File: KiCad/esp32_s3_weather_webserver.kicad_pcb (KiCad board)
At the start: 4 copper layers, 85 x 75 mm, 128 parts, among them IC301 CP2102N-A02-GQFN28R, IC401 ESP32-S3-WROOM-1-N16R8, IC501 VEML7700-TT, IC502 DS3231MZ+TRL, J201 Barrel_Jack_Switch_Pin3Ring, J301 USB_C_Receptacle_USB2.0, J302 USB_C_Receptacle_USB2.0, J401 Conn_01x04_Pin, J402 Conn_01x04_Pin, J403 Conn_01x04_Pin, J404 TF-01A, J405 Conn_01x08_Pin, Q401 SS8050, Q402 SS8050, U201 AMS1117-3.3, U202 TLV62569DBV, U301 USBLC6-2SC6, U302 USBLC6-2SC6, U502 DS18B20, U503 LM35-LP, U504 DHT11

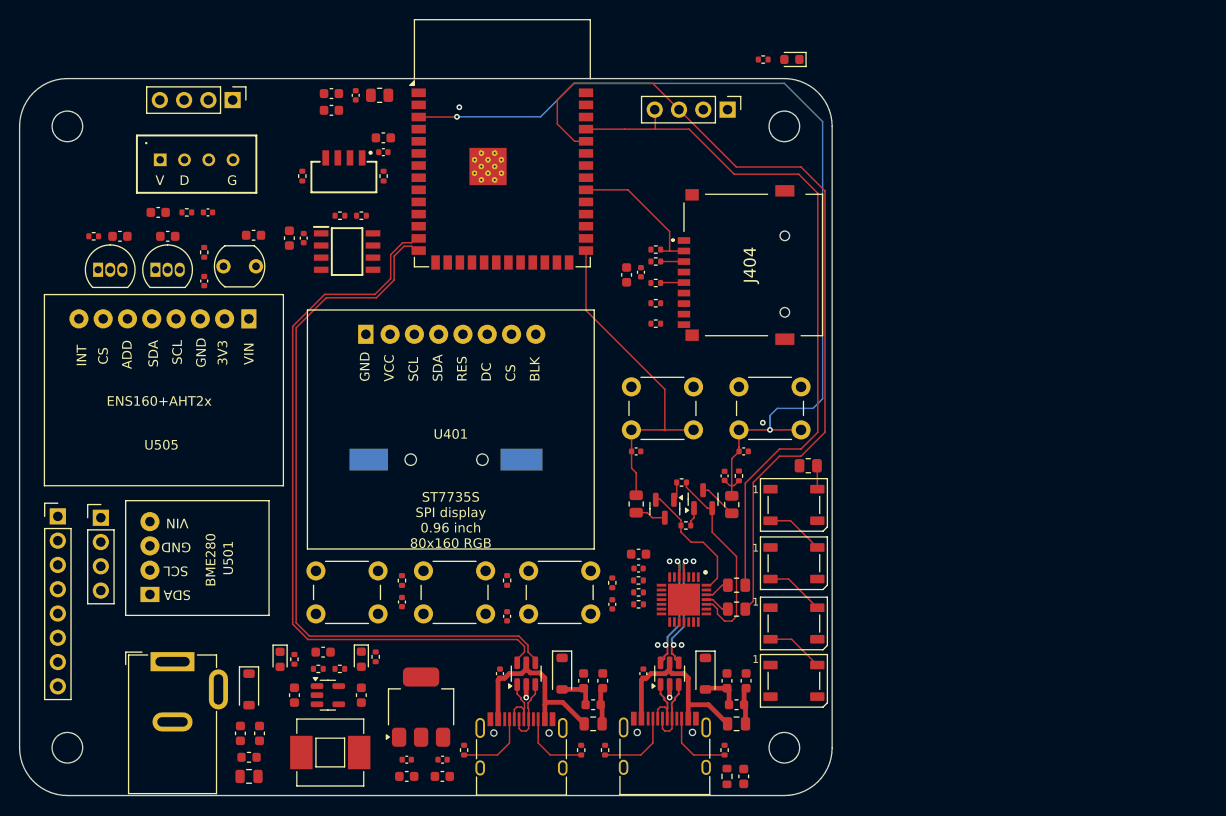
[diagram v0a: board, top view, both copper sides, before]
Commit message: SPI signals routing
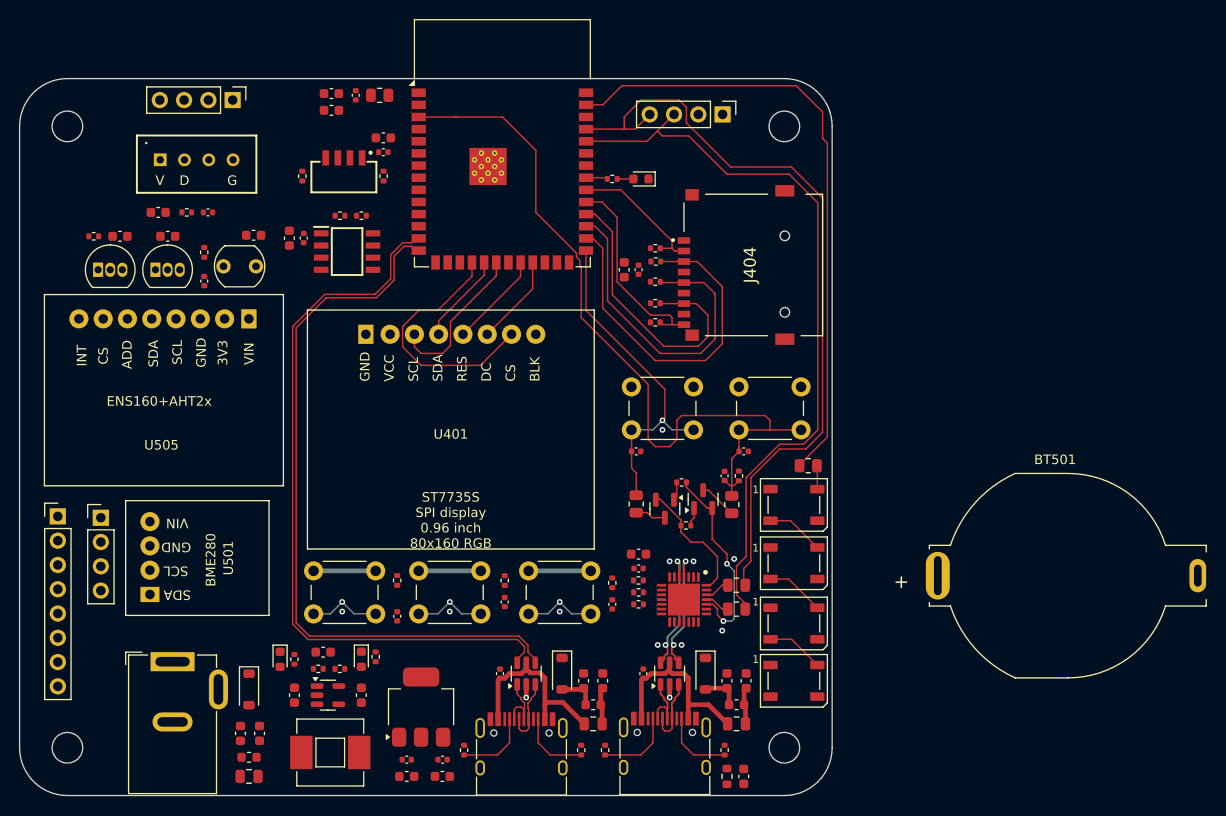
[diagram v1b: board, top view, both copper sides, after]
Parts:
- BT501: footprint esp32_s3_weather_webserver:CR12202 -> esp32_s3_weather_webserver:MPD_BC2032-E2; moved to F.Cu
- moved BT501 66.3 mm to (134.7, 77.0)
- moved D210 20.1 mm to (90.0, 35.5)
- moved R206 20.1 mm to (87.0, 35.5)
- moved C512 11.5 mm to (64.5, 81.2)
- moved R509 11.5 mm to (64.5, 77.5)
- moved SW502 11.5 mm to (55.8, 76.5)
- moved C511 10.8 mm to (75.8, 79.8)
- moved R508 10.8 mm to (75.8, 77.5)
- moved SW501 10.8 mm to (66.8, 76.5)
- moved J402 0.72 mm to (98.5, 28.8)
- moved C407 0.59 mm to (88.2, 45.0), turned to -90 degrees
- moved C408 0.36 mm to (89.8, 45.0), turned to -90 degrees
- moved R411 0.14 mm to (91.5, 46.2)
- moved R412 0.14 mm to (91.5, 42.8)
- moved R413 0.14 mm to (91.5, 50.5)
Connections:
- IC401 pad 10: USR_BTN_LEFT -> ENS160_INT
- IC401 pad 11: USR_BTN_RIGHT -> DS3231_INT
- IC401 pad 22: ENS160_INT -> TFT_RES
- IC401 pad 23: SD_CD -> TFT_DC
- IC401 pad 25: WS2812_RGB_STRIP -> USR_BTN
- IC401 pad 31: ONBOARD_LED -> SD_CD
- IC401 pad 33: TFT_RES -> ONBOARD_LED
- IC401 pad 34: TFT_DC -> USR_BTN_RIGHT
- IC401 pad 35: DS3231_INT -> USR_BTN_LEFT
- IC401 pad 39: USR_BTN -> WS2812_RGB_STRIP
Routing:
- net WS2812_RGB_STRIP: track 0.00 -> 65.1 mm
- net FSPI_MOSI: track 2.44 -> 37.5 mm
- net FSPI_SCK: track 2.46 -> 34.5 mm
- net FSPI_MISO: track 0.00 -> 30.5 mm
- net HSPI_SS: track 0.00 -> 26.5 mm
- net SD_CD: track 0.00 -> 21.3 mm
- net +3V3_PER: track 0.00 -> 19.5 mm
- net HSPI_SCK: track 0.00 -> 16.4 mm
- net /[4] ESP32 S3/CHIP_PU: track 97.7 -> 81.5 mm, vias 2 -> 0
- net /[4] ESP32 S3/RXD0: track 88.2 -> 78.1 mm
- net TFT_RES: track 0.00 -> 10.0 mm
- net TFT_DC: track 0.00 -> 9.48 mm
- net HSPI_MOSI: track 0.00 -> 9.48 mm
- net USR_BTN_RIGHT: track 0.00 -> 7.54 mm, vias 0 -> 1
- net USR_BTN_LEFT: track 0.00 -> 7.54 mm, vias 0 -> 1
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
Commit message: Simple signal routing
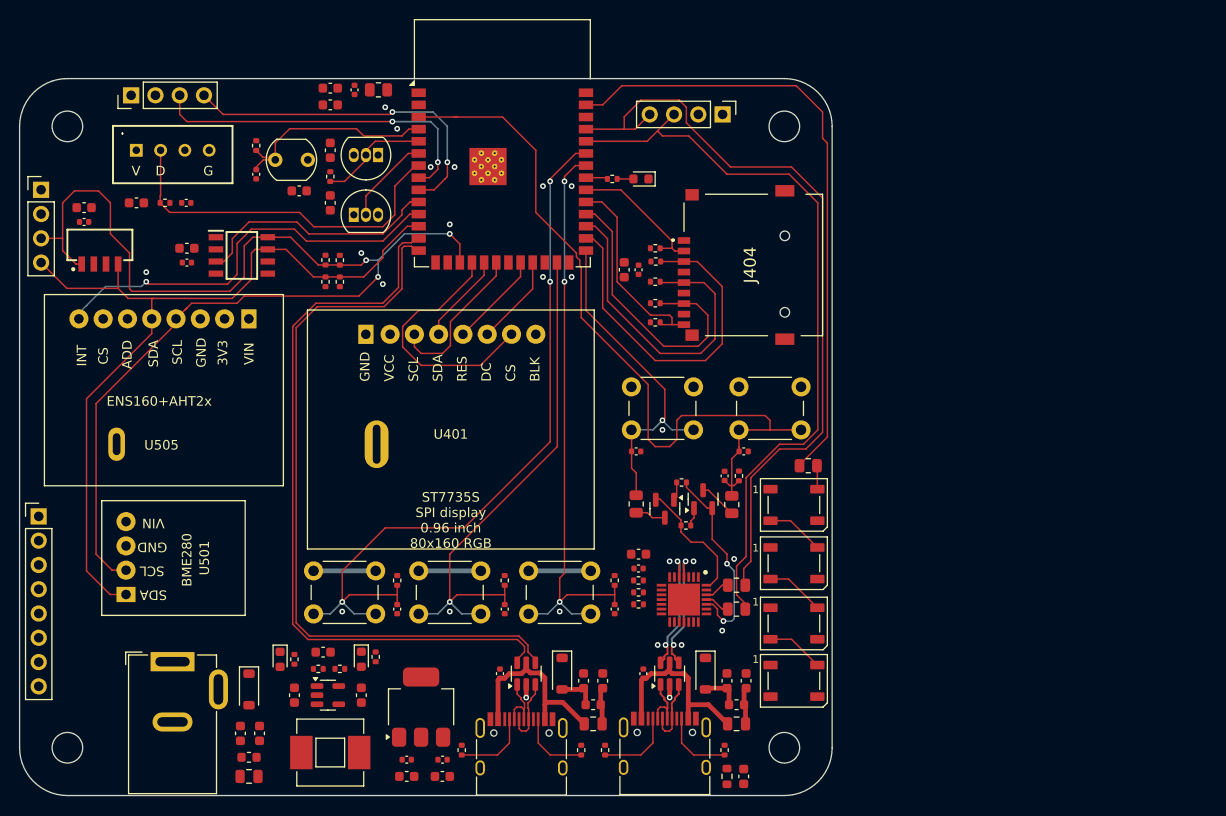
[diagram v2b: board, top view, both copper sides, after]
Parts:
- BT501: moved to B.Cu
- moved BT501 87.0 mm to (48.8, 63.2), turned to 180 degrees
- moved J403 34.9 mm to (27.2, 36.6)
- moved IC501 33.9 mm to (30.0, 44.0), turned to 0 degrees
- moved C503 32.1 mm to (31.8, 38.5)
- moved C504 32.1 mm to (31.8, 40.0)
- moved U502 31.7 mm to (62.5, 33.0), turned to 180 degrees
- moved R504 25.5 mm to (57.5, 35.2), turned to -90 degrees
- moved C505 23.8 mm to (57.5, 32.5), turned to 90 degrees
- moved U503 21.5 mm to (60.0, 39.2)
- moved C506 17.4 mm to (57.5, 38.0), turned to 90 degrees
- moved C508 12.5 mm to (42.5, 44.2), turned to 0 degrees
- moved C502 12.4 mm to (49.8, 35.0)
- moved R501 12.4 mm to (49.8, 32.0)
- moved RLO501 12.4 mm to (51.8, 33.5)
- moved R503 11.3 mm to (57.0, 46.3)
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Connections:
- IC401 pad 10: ENS160_INT -> DS3231_INT
- IC401 pad 11: DS3231_INT -> ENS160_INT
- J403 pad 3: I2C_SDA -> I2C_SCL
- J403 pad 4: I2C_SCL -> I2C_SDA
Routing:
- net I2C_SCL: track 0.00 -> 126.7 mm, vias 0 -> 3
- net I2C_SDA: track 0.00 -> 87.8 mm
- net USR_BTN_LEFT: track 7.54 -> 78.7 mm, vias 1 -> 3
- net USR_BTN_RIGHT: track 7.54 -> 63.0 mm, vias 1 -> 3
- net USR_BTN: track 7.54 -> 55.8 mm
- net ENS160_INT: track 0.00 -> 43.6 mm, vias 0 -> 1
- net DHT11: track 0.00 -> 38.0 mm
- net RXD1: track 0.00 -> 36.2 mm, vias 0 -> 2
- net TXD1: track 0.00 -> 35.8 mm, vias 0 -> 2
- net DS3231_INT: track 0.00 -> 26.0 mm
- net LDR: track 0.00 -> 23.0 mm
- net DS18B20: track 0.00 -> 11.6 mm
- net LM35: track 0.00 -> 9.34 mm
- net USB_D+: track 76.2 -> 77.3 mm
- net USB_D-: track 76.8 -> 77.9 mm
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
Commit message: Signals routing
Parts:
- moved D209 19.0 mm to (33.2, 84.5)
- moved R205 19.0 mm to (34.8, 84.5)
- moved D201 18.8 mm to (67.8, 89.2)
- moved F201 18.8 mm to (67.8, 98.2)
- moved FB201 18.8 mm to (67.8, 96.2)
- moved J201 18.8 mm to (59.8, 86.2)
- moved C205 18.7 mm to (68.8, 93.8)
- moved C206 18.7 mm to (66.8, 93.8)
- moved C202 18.0 mm to (51.2, 96.5), turned to 180 degrees
- moved C203 18.0 mm to (47.5, 96.5), turned to 0 degrees
- moved C204 18.0 mm to (47.5, 98.2), turned to 0 degrees
- moved C207 18.0 mm to (42.8, 89.8)
- moved C208 18.0 mm to (35.8, 89.8)
- moved C209 18.0 mm to (38.8, 85.2)
- moved L201 18.0 mm to (39.5, 95.8)
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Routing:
- net +5V: track 0.00 -> 250.2 mm, vias 0 -> 10
- net +3V3: track 0.00 -> 55.9 mm
- net GNDPWR: track 0.00 -> 44.4 mm
- net GND: track 2.72 -> 46.1 mm, vias 24 -> 80
- net +3V3_PER: track 19.5 -> 60.7 mm
- net /[5] Peripherals/VBAT: track 0.00 -> 32.2 mm, vias 0 -> 1
- net +VCC_USB2UART_FILT: track 4.11 -> 21.8 mm
- net +5V_IN: track 0.00 -> 16.0 mm
- net I2C_SCL: track 126.7 -> 113.2 mm, vias 3 -> 4
- net +5V_IN_FILT: track 0.00 -> 9.65 mm
- net /[2] Power/BUCK_FB: track 0.00 -> 5.45 mm
- net I2C_SDA: track 87.8 -> 92.2 mm
- net +5V_IN_FUSE: track 0.00 -> 3.88 mm
- net /[3] USB/VBUS: track 0.00 -> 3.14 mm
- net /[3] USB/RSTB: track 0.00 -> 2.95 mm
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- added copper zone on F.Cu, net +3V3_PER
- added copper zone on F.Cu, net /[2] Power/BUCK_SW

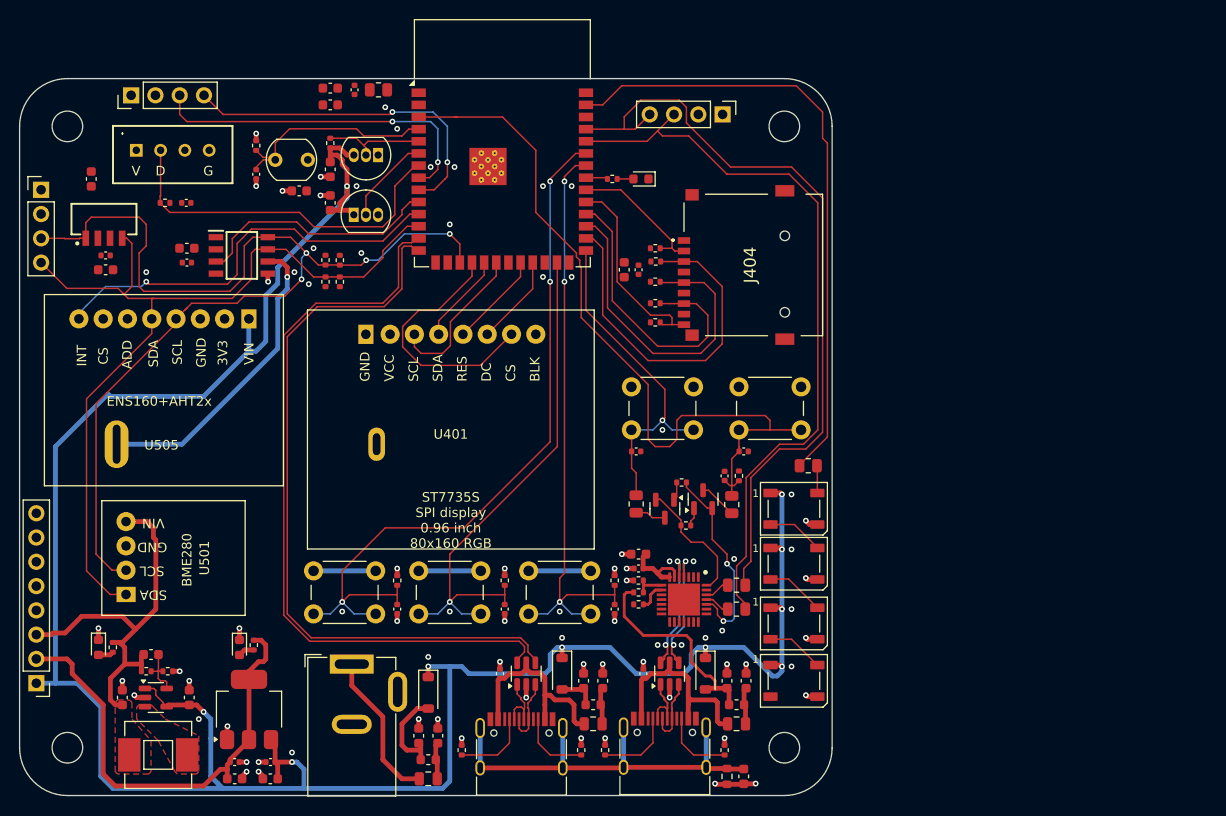
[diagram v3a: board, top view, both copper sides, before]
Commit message: Signal routing
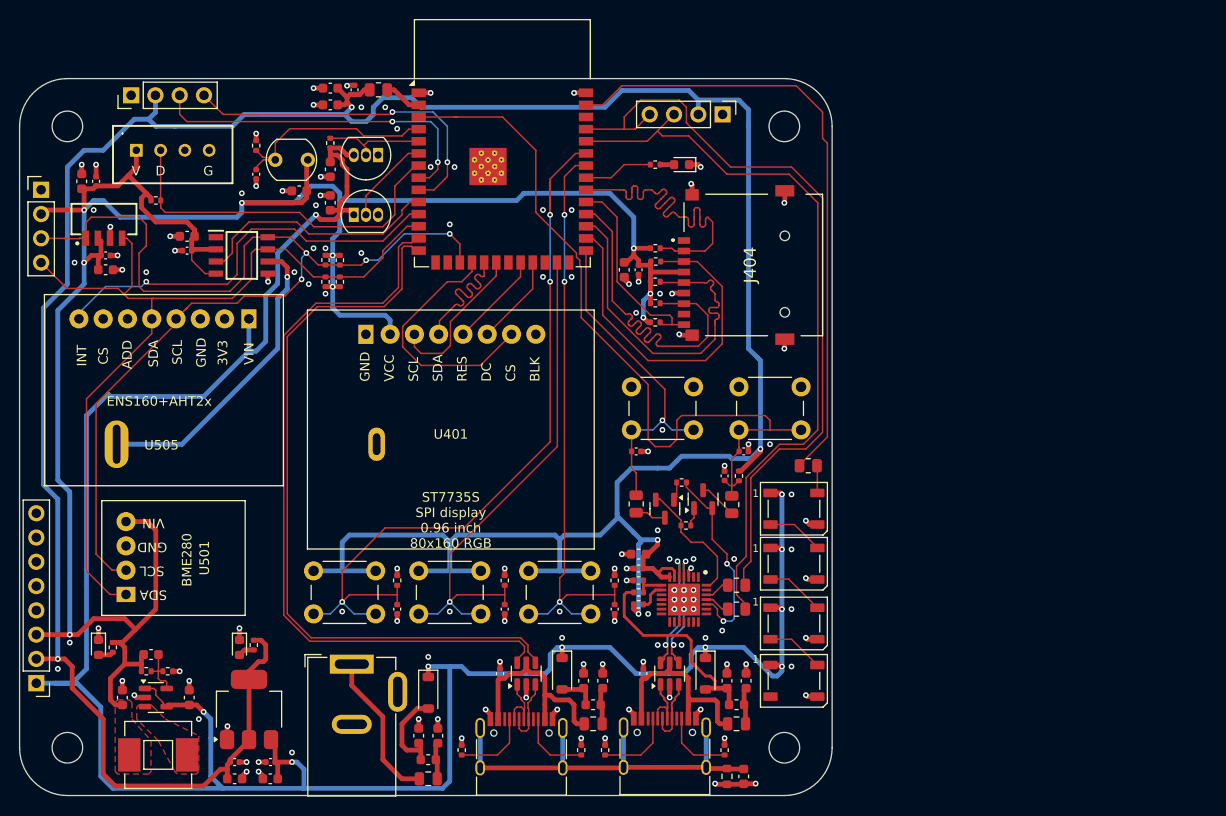
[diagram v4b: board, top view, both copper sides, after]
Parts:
- moved C510 9.70 mm to (33.0, 35.8), turned to 90 degrees
- moved R206 4.73 mm to (91.5, 34.0)
- moved D210 4.51 mm to (94.2, 34.0)
- moved C507 1.25 mm to (42.5, 41.5), turned to 180 degrees
- moved C508 1.25 mm to (42.5, 43.0), turned to 180 degrees
- moved C509 1.03 mm to (31.5, 35.8)
- moved R505 1.00 mm to (39.2, 37.8), turned to 0 degrees
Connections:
- SW501 pad 1: +3V3_PER -> +3V3
- SW501 pad 4: +3V3_PER -> +3V3
- SW502 pad 1: +3V3_PER -> +3V3
- SW502 pad 4: +3V3_PER -> +3V3
- SW503 pad 1: +3V3_PER -> +3V3
- SW503 pad 4: +3V3_PER -> +3V3
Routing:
- net +3V3: track 55.9 -> 334.3 mm, vias 0 -> 5
- net +3V3_PER: track 60.7 -> 246.9 mm, vias 0 -> 9
- net GND: track 46.1 -> 75.5 mm, vias 80 -> 130
- net FSPI_SS: track 14.6 -> 38.7 mm
- net FSPI_MISO: track 30.9 -> 37.6 mm
- net HSPI_MOSI: track 9.48 -> 15.5 mm
- net ONBOARD_LED: track 2.29 -> 7.30 mm
- net +3V3_ESP32: track 0.00 -> 3.95 mm
- net USR_BTN_LEFT: track 78.7 -> 82.1 mm
- net FSPI_SCK: track 35.0 -> 38.1 mm

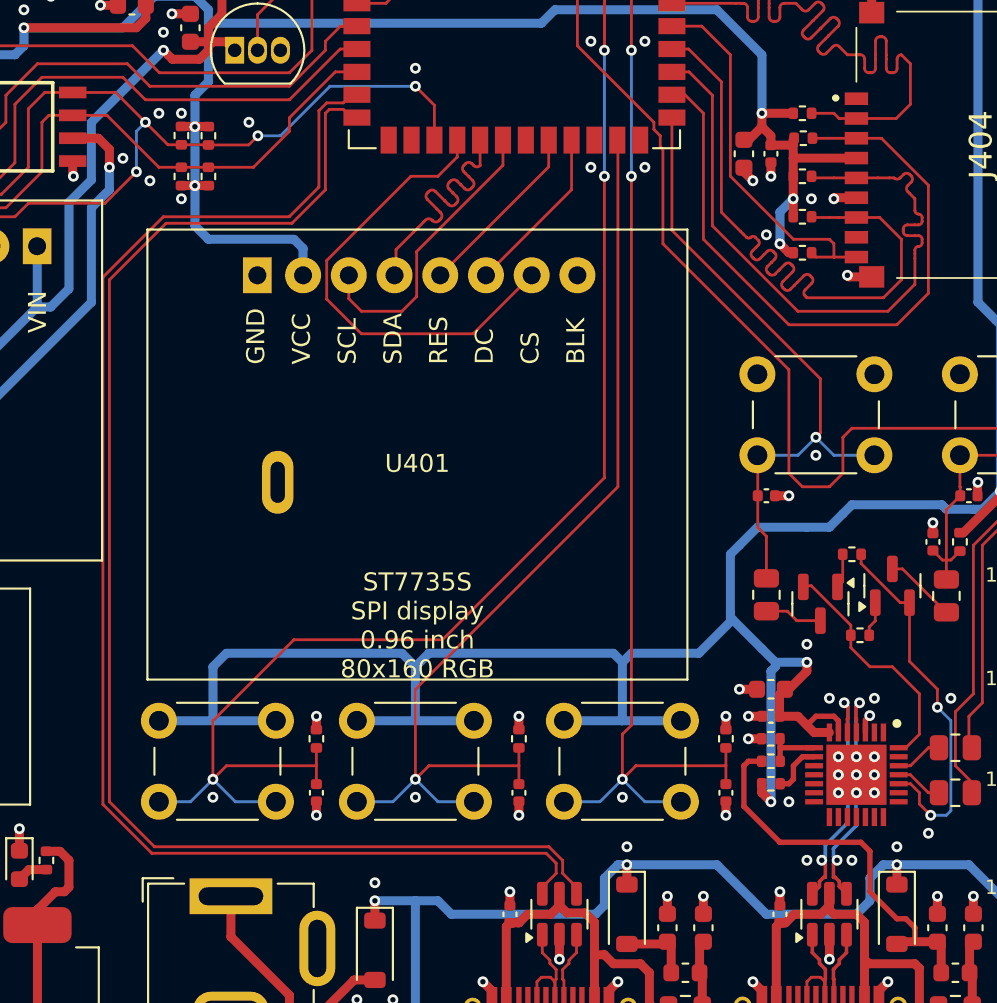
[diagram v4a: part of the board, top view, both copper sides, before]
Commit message: Fix USB signal routing
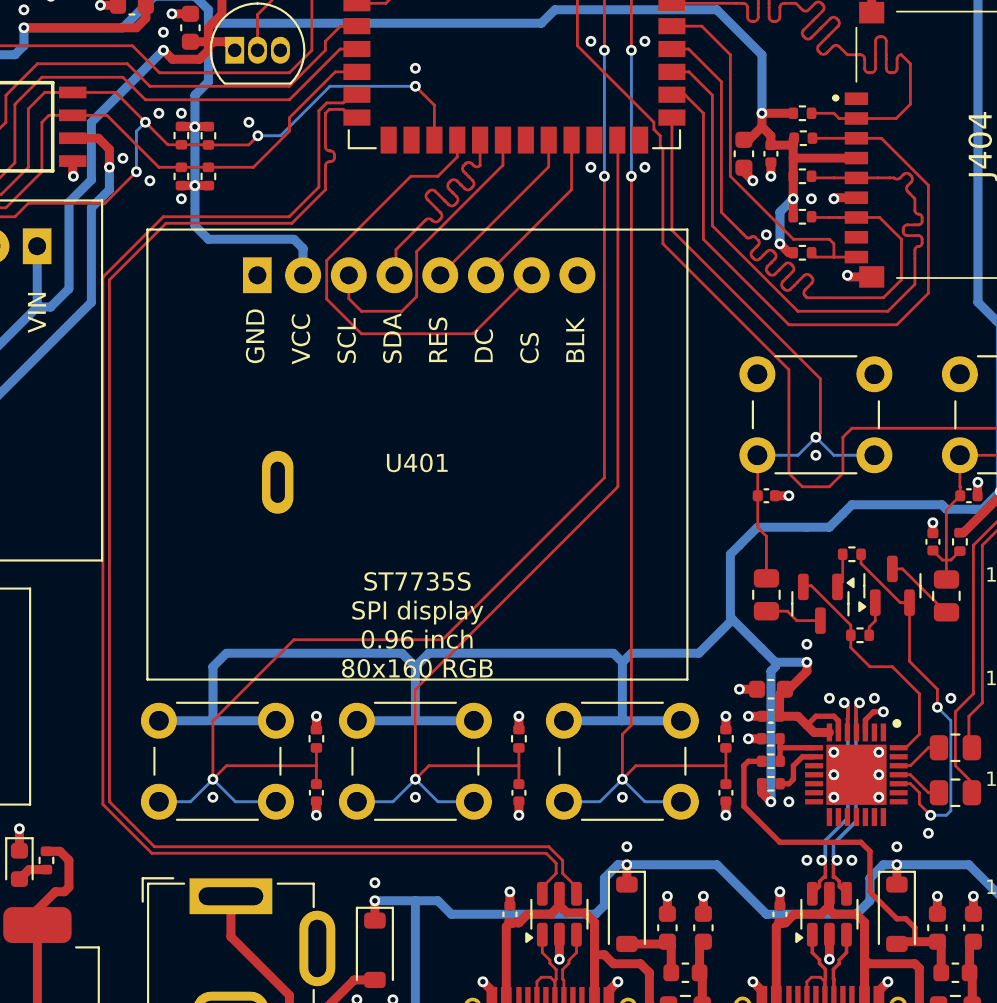
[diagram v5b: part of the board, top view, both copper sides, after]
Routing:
- net GND: track 75.5 -> 76.3 mm, vias 130 -> 127
- net USB_D+: track 78.0 -> 78.6 mm

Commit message: Fix DRC
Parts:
- added R414: 0R, Resistor_SMD:R_0805_2012Metric, F.Cu at (78.5, 47.8)
- J405: value Conn_01x08_Pin -> Conn_01x06_Pin; footprint Connector_PinHeader_2.54mm:PinHeader_1x08_P2.54mm_Vertical -> Connector_PinHeader_2.54mm:PinHeader_1x06_P2.54mm_Vertical
- moved J201 0.38 mm to (59.6, 85.9)
- moved J405 0.25 mm to (27.0, 88.3)
- moved J302 0.06 mm to (77.5, 96.0)
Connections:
- IC401 pad 24: GPIO47 -> TFT_BLK
- IC401 pad 38: GPIO2 -> unconnected-(IC401-IO2-Pad38)
- J405 pad 2: +3V3 -> GND
- J405 pad 3: +3V3_PER -> +3V3
- J405 pad 5: GPIO2 -> +3V3_PER
- U401 pad 8: unconnected-(U401-BLK-Pad8) -> Net-(U401-BLK)
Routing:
- net TFT_BLK: track 0.00 -> 4.49 mm
- net Net-(U401-BLK): track 0.00 -> 4.17 mm
- net +3V3_PER: track 246.9 -> 242.9 mm
- net WS2812_RGB_STRIP: track 65.1 -> 63.5 mm
- net +3V3: track 334.3 -> 333.7 mm
- net GND: track 76.3 -> 76.1 mm, vias 127 -> 258
- added copper zone on B.Cu, net GND
- added copper zone on F.Cu, net GND
